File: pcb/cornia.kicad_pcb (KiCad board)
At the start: 2 copper layers, 159.3 x 108.3 mm, 60 parts, among them SW1 SW_Push, SW10 SW_Push, SW11 SW_Push, SW12 SW_Push, SW13 SW_Push, SW14 SW_Push, SW15 SW_Push, SW16 SW_Push, SW17 SW_Push, SW18 SW_Push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

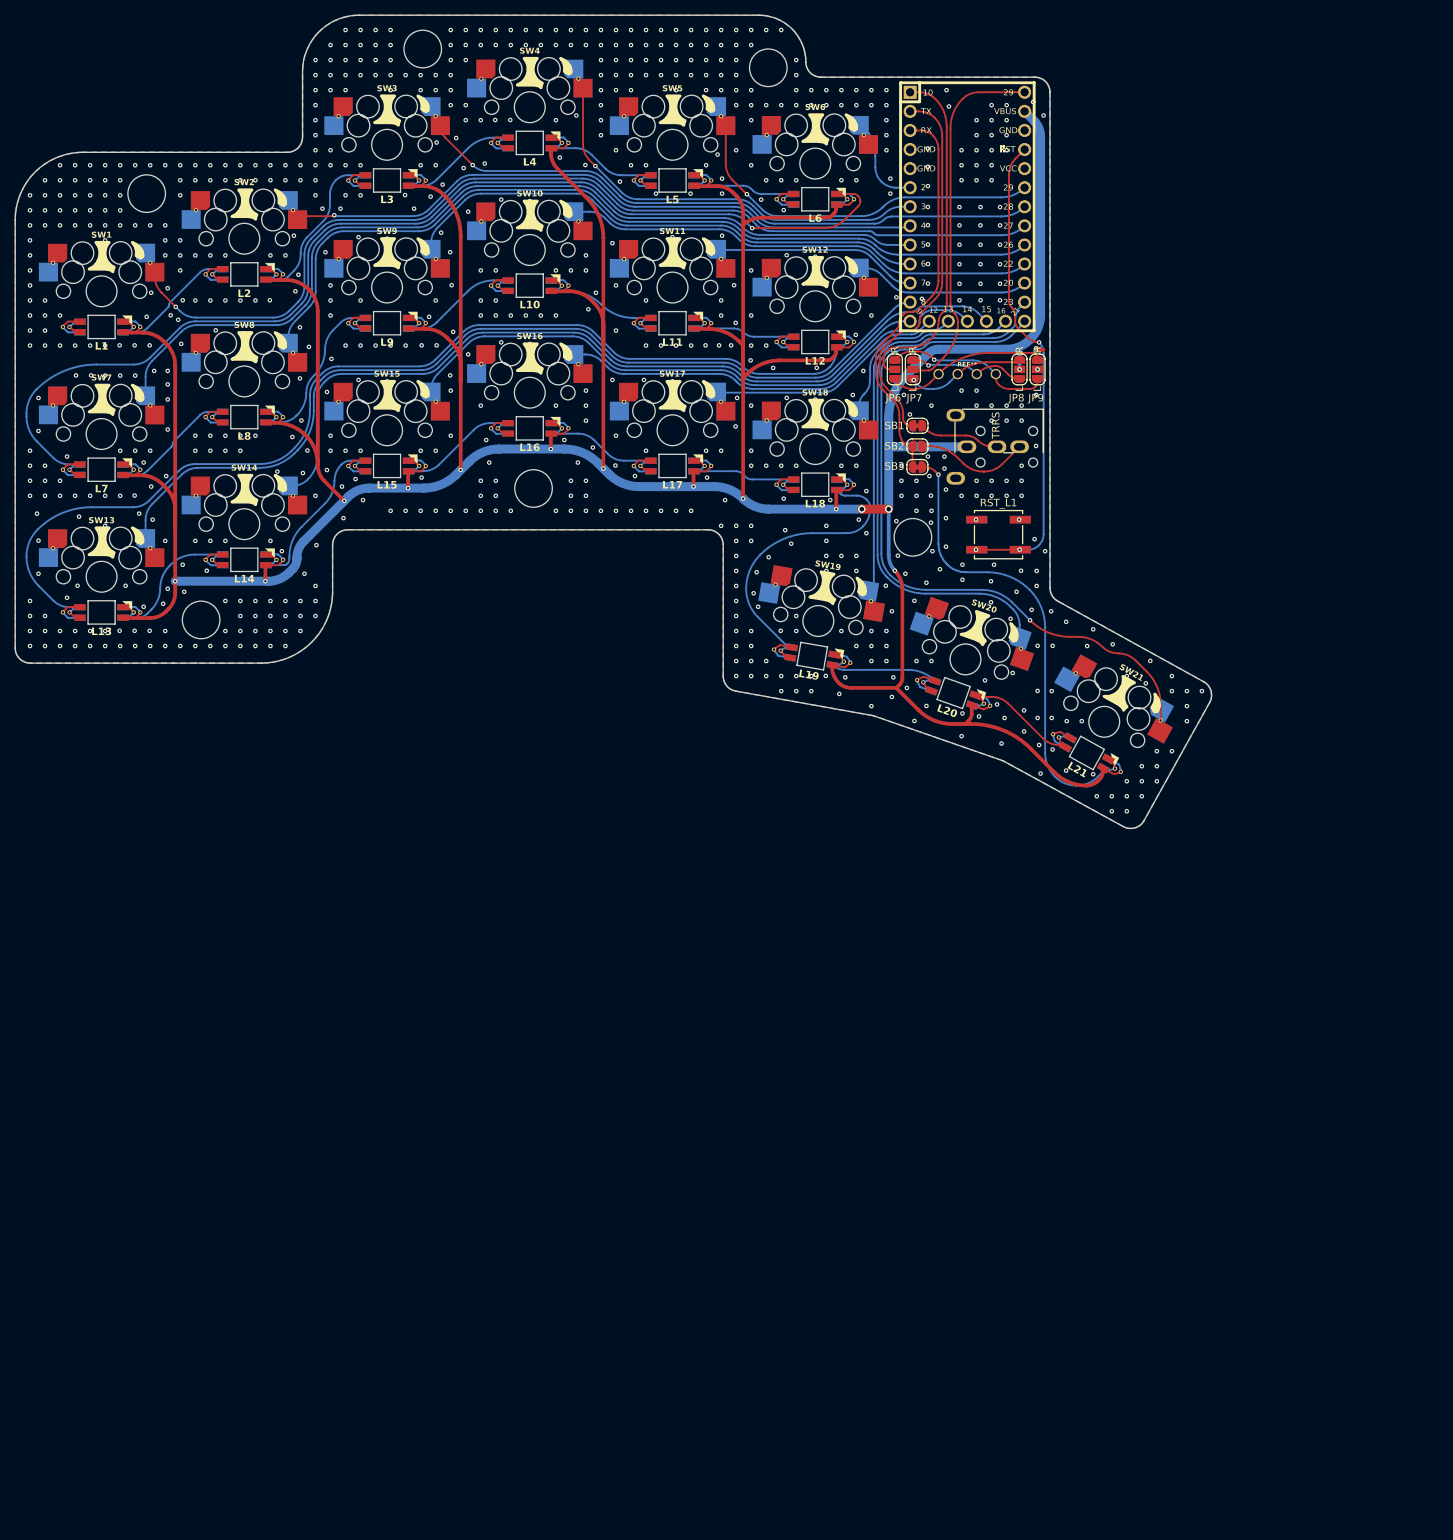
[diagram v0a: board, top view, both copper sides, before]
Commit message: Finish routing & add gerber/case export in CLI
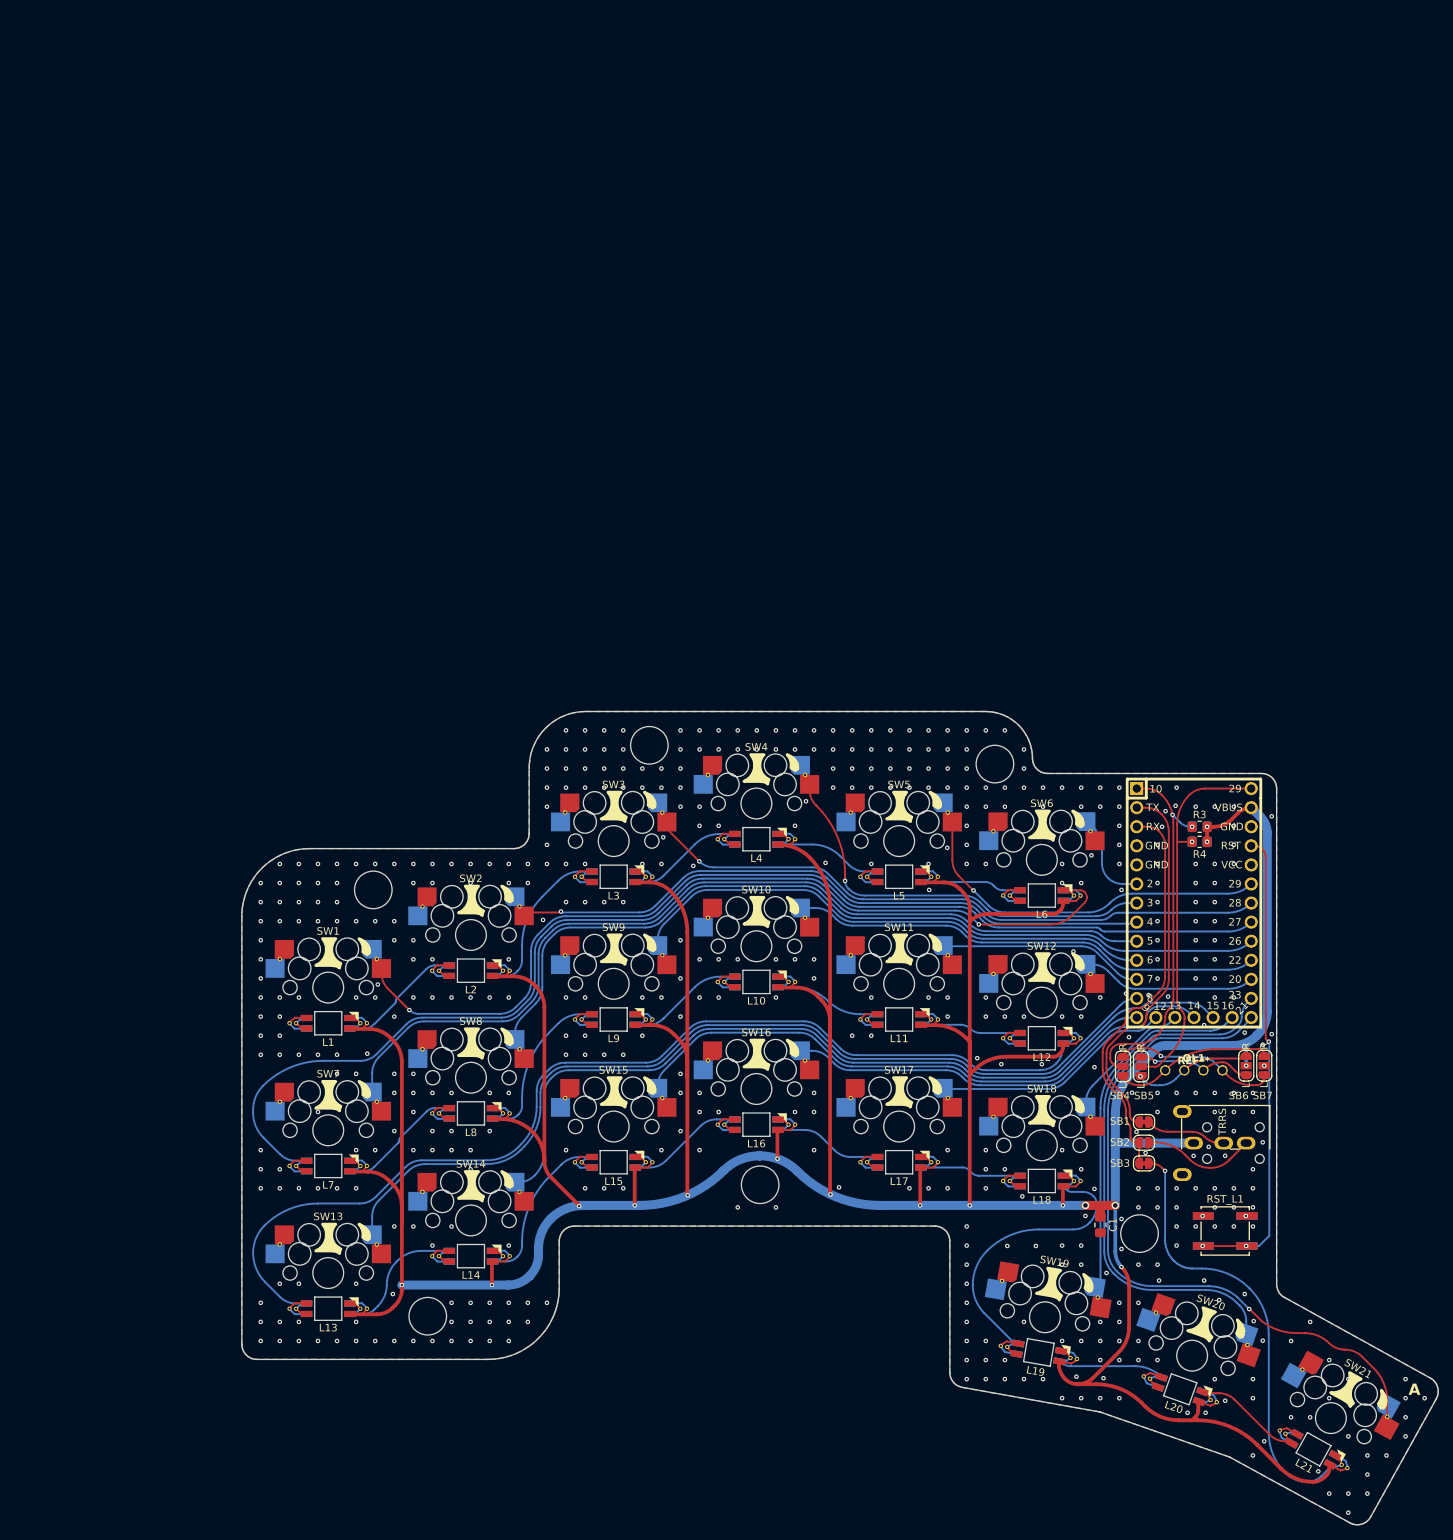
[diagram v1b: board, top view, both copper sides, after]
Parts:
- removed JP6, JP7, JP8, JP9: SB, cornia-footprints:SolderJumper-3
- added C1: 1uF, cornia-footprints:C_0805, F.Cu at (133.0, 86.3)
- added R1: 2.2k, cornia-footprints:R_0805, B.Cu at (146.2, 33.3)
- added R2: 2.2k, cornia-footprints:R_0805, B.Cu at (146.2, 35.3)
- added R3: 2.2k, cornia-footprints:R_0805, F.Cu at (146.2, 33.3)
- added R4: 2.2k, cornia-footprints:R_0805, F.Cu at (146.2, 35.3)
- added SB4: SB, cornia-footprints:SolderJumper-3, F.Cu at (136.0, 65.2)
- added SB5: SB, cornia-footprints:SolderJumper-3, F.Cu at (138.4, 65.2)
- added SB6: SB, cornia-footprints:SolderJumper-3, F.Cu at (152.4, 65.1)
- added SB7: SB, cornia-footprints:SolderJumper-3, F.Cu at (154.8, 65.1)
- SB1, SB3: footprint Jumper:SolderJumper-2_P1.3mm_Bridged_RoundedPad1.0x1.5mm -> cornia-footprints:SolderJumper-2_Bridged
- SB2: footprint Jumper:SolderJumper-2_P1.3mm_Open_RoundedPad1.0x1.5mm -> cornia-footprints:SolderJumper-2_Open
- moved L20 97.5 mm to (143.6, 108.2)
- moved H1 97.5 mm to (43.4, 98.4)
- moved H2 97.5 mm to (87.7, 80.9)
- moved H3 97.5 mm to (138.2, 87.4)
- moved H4 97.5 mm to (36.2, 41.7)
- moved H5 97.5 mm to (72.9, 22.4)
- moved H6 97.5 mm to (118.9, 24.9)
- moved L1 97.5 mm to (30.2, 59.4)
- moved L10 97.5 mm to (87.2, 53.9)
- moved L11 97.5 mm to (106.2, 58.9)
- moved L12 97.5 mm to (125.2, 61.4)
- moved L13 97.5 mm to (30.2, 97.4)
- moved L14 97.5 mm to (49.2, 90.4)
- moved L15 97.5 mm to (68.2, 77.9)
- moved L16 97.5 mm to (87.2, 72.9)
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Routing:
- net VBUS: track 571.7 -> 605.0 mm, vias 14 -> 16
- net /SDA: track 46.5 -> 49.8 mm, vias 0 -> 2
- net /In_SW20: track 74.1 -> 72.0 mm
- net /In_SW19: track 50.1 -> 48.0 mm
- net /In_SW21: track 94.3 -> 92.3 mm
- net /SCL: track 48.7 -> 50.7 mm, vias 0 -> 1
- net /In_SW18: track 19.2 -> 17.6 mm
- net /RST: track 64.2 -> 62.9 mm
- net /LED: track 60.3 -> 59.1 mm
- net GND: track 1.08 -> 0.00 mm, vias 814 -> 522
- net /In_SW4: track 55.8 -> 55.1 mm
- net Net-(OL1-GND): track 22.4 -> 21.7 mm
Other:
- board text added: "A"
- board text added: "B"
- board text added: "TRRS"
- board text removed: "REF**"
